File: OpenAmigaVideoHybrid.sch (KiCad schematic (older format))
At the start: 52 parts, among them J1 Conn_01x22, J99 OSHW_LOGO, Q1 2N3904, Q2 2N3904, Q3 2N3904, Q4 2N3904, Q5 2N3904, Q6 2N3906

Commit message: Begin migrating project to KiCad 5
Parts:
- removed C1, C2, C3, C4, C5: 100n, Capacitors_SMD:C_0805_HandSoldering, symbol C
- removed J1: Conn_01x22, OpenAmigaVideoHybrid:Pin_Header_Straight_1x22_Pitch2.54mm, symbol Conn_01x22
- removed J99: OSHW_LOGO, w_logo:Logo_copper_OSHW_6x6mm, symbol Conn_01x01
- removed Q1, Q2, Q3, Q4, Q5: 2N3904, OpenAmigaVideoHybrid:2N3904_2N3906_SOT-23, symbol 2N3904
- removed Q6: 2N3906, OpenAmigaVideoHybrid:2N3904_2N3906_SOT-23, symbol 2N3906
- removed R1, R17, R25, R9: 1k, Resistors_SMD:R_0805_HandSoldering, symbol R
- removed R10, R18, R2: 2k, Resistors_SMD:R_0805_HandSoldering, symbol R
- removed R11, R19, R3: 4k, Resistors_SMD:R_0805_HandSoldering, symbol R
- removed R12, R20, R4: 8k, Resistors_SMD:R_0805_HandSoldering, symbol R
- removed R13, R21, R5: 470, Resistors_SMD:R_0805_HandSoldering, symbol R
- removed R14, R22, R6: 390, Resistors_SMD:R_0805_HandSoldering, symbol R
- removed R15, R16, R23, R24, R29, R39, R7, R8: 75, Resistors_SMD:R_0805_HandSoldering, symbol R
- removed R26, R36: 220, Resistors_SMD:R_0805_HandSoldering, symbol R
- removed R27: 27k, Resistors_SMD:R_0805_HandSoldering, symbol R
- removed R28: 150, Resistors_SMD:R_0805_HandSoldering, symbol R
- removed R30: 90.9k, Resistors_SMD:R_0805_HandSoldering, symbol R
- removed R31, R34: 37.4k, Resistors_SMD:R_0805_HandSoldering, symbol R
- removed R32: 13.3k, Resistors_SMD:R_0805_HandSoldering, symbol R
- removed R33: 6.04k, Resistors_SMD:R_0805_HandSoldering, symbol R
- removed R35: 19.6k, Resistors_SMD:R_0805_HandSoldering, symbol R
- removed R37, R38: 36, Resistors_SMD:R_0805_HandSoldering, symbol R
- added C1, C2, C3, C4, C5: 100n, Capacitor_SMD:C_0805_2012Metric_Pad1.15x1.40mm_HandSolder, symbol Device:C
- added J1: CONN_MAINBOARD, Connector_PinHeader_2.54mm:PinHeader_1x22_P2.54mm_Vertical, symbol Connector:Conn_01x22_Male
- added Q1, Q2, Q3, Q4, Q5: 2N3904, OpenAmigaVideoHybrid:2N3904_2N3906_SOT-23, symbol Transistor_BJT:2N3904
- added Q6: 2N3906, OpenAmigaVideoHybrid:2N3904_2N3906_SOT-23, symbol Transistor_BJT:2N3906
- added R1, R17, R25, R9: 1k, Resistor_SMD:R_0805_2012Metric_Pad1.15x1.40mm_HandSolder, symbol Device:R
- added R10, R18, R2: 2k, Resistor_SMD:R_0805_2012Metric_Pad1.15x1.40mm_HandSolder, symbol Device:R
- added R11, R19, R3: 4k, Resistor_SMD:R_0805_2012Metric_Pad1.15x1.40mm_HandSolder, symbol Device:R
- added R12, R20, R4: 8k, Resistor_SMD:R_0805_2012Metric_Pad1.15x1.40mm_HandSolder, symbol Device:R
- added R13, R21, R5: 470, Resistor_SMD:R_0805_2012Metric_Pad1.15x1.40mm_HandSolder, symbol Device:R
- added R14, R22, R6: 390, Resistor_SMD:R_0805_2012Metric_Pad1.15x1.40mm_HandSolder, symbol Device:R
- added R15, R16, R23, R24, R29, R39, R7, R8: 75, Resistor_SMD:R_0805_2012Metric_Pad1.15x1.40mm_HandSolder, symbol Device:R
- added R26, R36: 220, Resistor_SMD:R_0805_2012Metric_Pad1.15x1.40mm_HandSolder, symbol Device:R
- added R27: 27k, Resistor_SMD:R_0805_2012Metric_Pad1.15x1.40mm_HandSolder, symbol Device:R
- added R28: 150, Resistor_SMD:R_0805_2012Metric_Pad1.15x1.40mm_HandSolder, symbol Device:R
- added R30: 90.9k, Resistor_SMD:R_0805_2012Metric_Pad1.15x1.40mm_HandSolder, symbol Device:R
- added R31, R34: 37.4k, Resistor_SMD:R_0805_2012Metric_Pad1.15x1.40mm_HandSolder, symbol Device:R
- added R32: 13.3k, Resistor_SMD:R_0805_2012Metric_Pad1.15x1.40mm_HandSolder, symbol Device:R
- added R33: 6.04k, Resistor_SMD:R_0805_2012Metric_Pad1.15x1.40mm_HandSolder, symbol Device:R
- added R35: 19.6k, Resistor_SMD:R_0805_2012Metric_Pad1.15x1.40mm_HandSolder, symbol Device:R
- added R37, R38: 36, Resistor_SMD:R_0805_2012Metric_Pad1.15x1.40mm_HandSolder, symbol Device:R
- added V0: OSHW_LOGO, Symbol:OSHW-Logo_5.7x6mm_Copper, symbol void:Void
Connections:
- wire segments 141 -> 197
- no-connect marks 1 -> 0

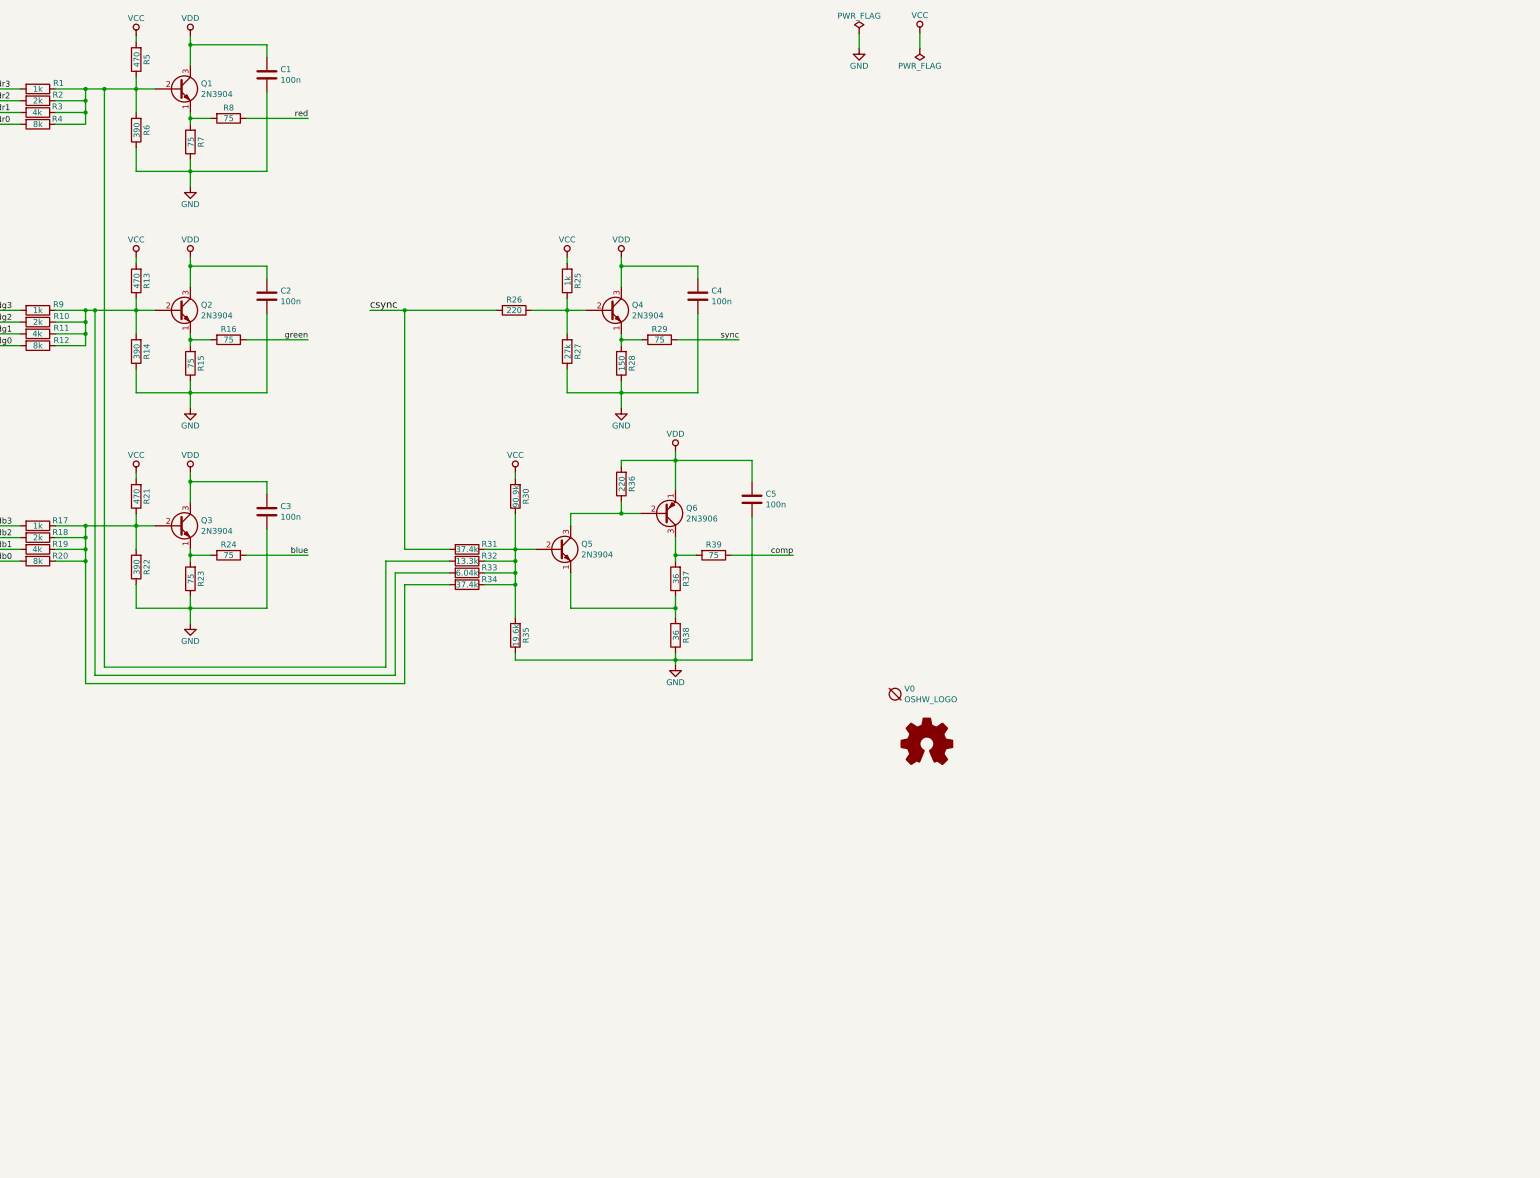
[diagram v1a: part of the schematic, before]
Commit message: Start working on color composite version
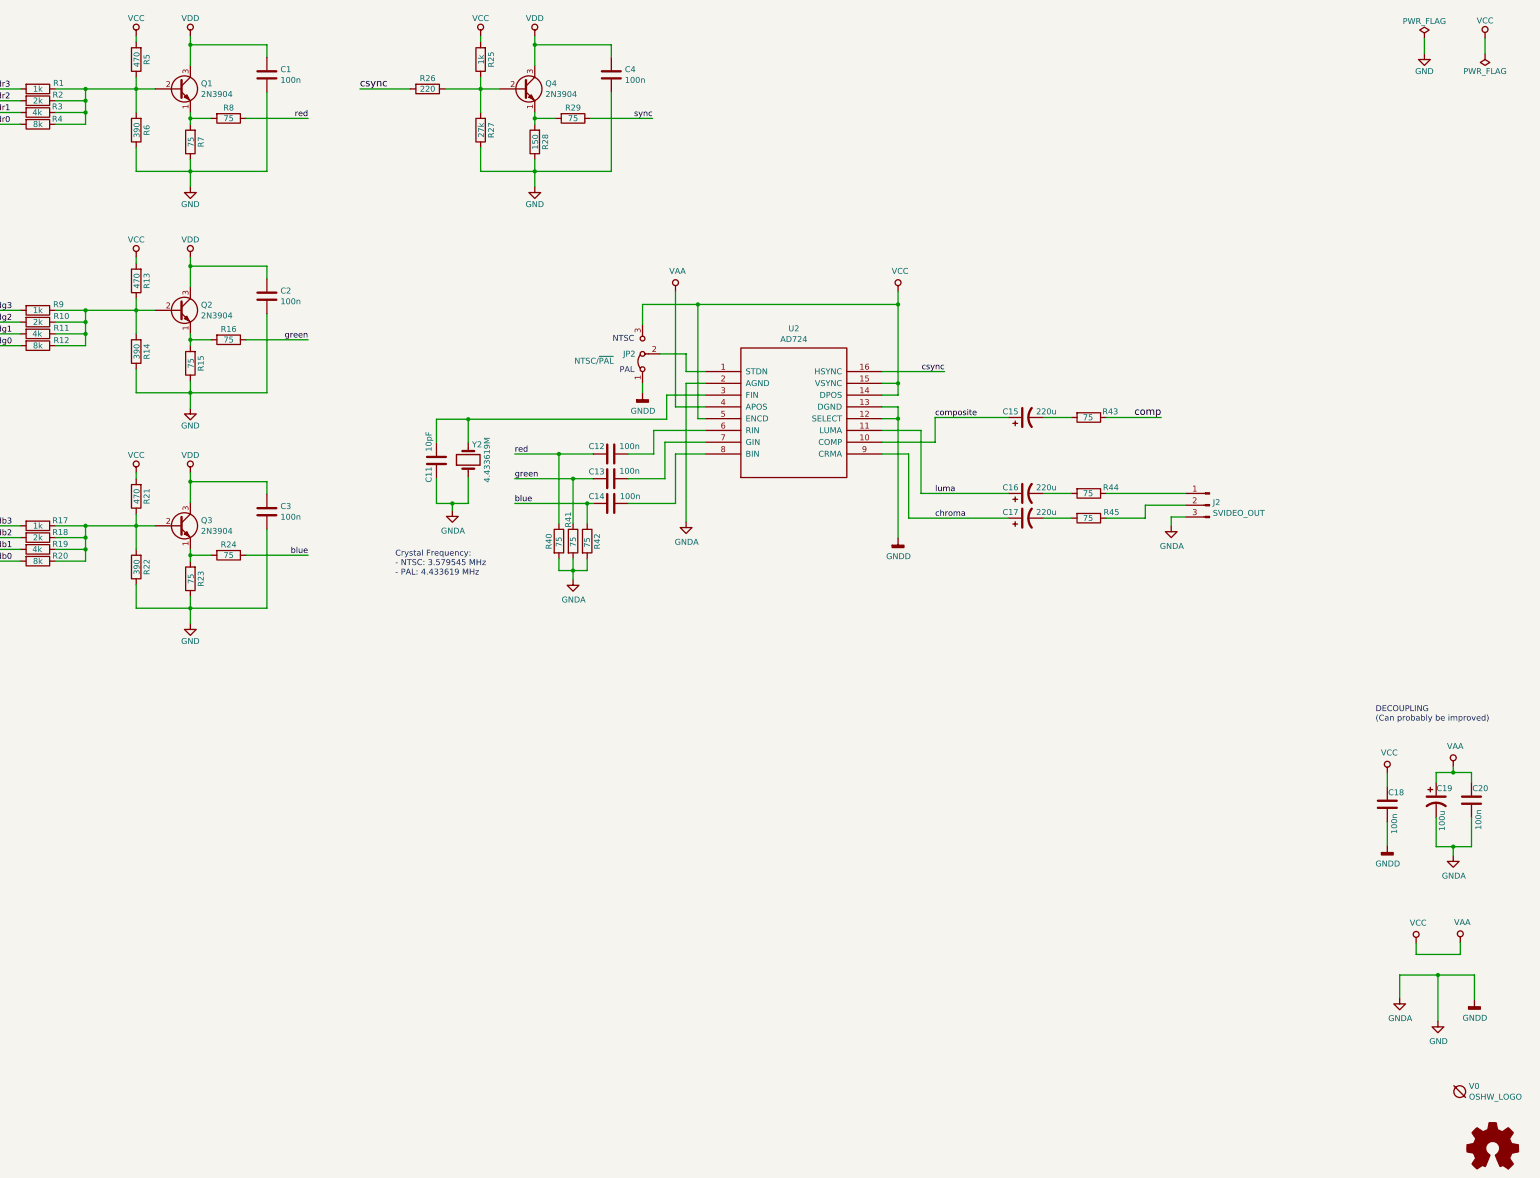
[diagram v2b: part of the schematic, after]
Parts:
- removed C5: 100n, Capacitor_SMD:C_0805_2012Metric_Pad1.15x1.40mm_HandSolder, symbol Device:C
- removed Q5: 2N3904, OpenAmigaVideoHybrid:2N3904_2N3906_SOT-23, symbol Transistor_BJT:2N3904
- removed Q6: 2N3906, OpenAmigaVideoHybrid:2N3904_2N3906_SOT-23, symbol Transistor_BJT:2N3906
- removed R30: 90.9k, Resistor_SMD:R_0805_2012Metric_Pad1.15x1.40mm_HandSolder, symbol Device:R
- removed R31, R34: 37.4k, Resistor_SMD:R_0805_2012Metric_Pad1.15x1.40mm_HandSolder, symbol Device:R
- removed R32: 13.3k, Resistor_SMD:R_0805_2012Metric_Pad1.15x1.40mm_HandSolder, symbol Device:R
- removed R33: 6.04k, Resistor_SMD:R_0805_2012Metric_Pad1.15x1.40mm_HandSolder, symbol Device:R
- removed R35: 19.6k, Resistor_SMD:R_0805_2012Metric_Pad1.15x1.40mm_HandSolder, symbol Device:R
- removed R36: 220, Resistor_SMD:R_0805_2012Metric_Pad1.15x1.40mm_HandSolder, symbol Device:R
- removed R37, R38: 36, Resistor_SMD:R_0805_2012Metric_Pad1.15x1.40mm_HandSolder, symbol Device:R
- removed R39: 75, Resistor_SMD:R_0805_2012Metric_Pad1.15x1.40mm_HandSolder, symbol Device:R
- added C11: 10pF, Capacitor_SMD:C_0805_2012Metric_Pad1.15x1.40mm_HandSolder, symbol Device:C
- added C12, C13, C14, C18: 100n, Capacitor_SMD:C_0805_2012Metric_Pad1.15x1.40mm_HandSolder, symbol Device:C
- added C15, C16, C17: 220u, Capacitor_SMD:CP_Elec_6.3x7.7, symbol Device:CP1
- added C19: 100u, Capacitor_SMD:CP_Elec_6.3x5.8, symbol Device:CP1
- added C20: 100n, Capacitor_SMD:C_1206_3216Metric_Pad1.42x1.75mm_HandSolder, symbol Device:C
- added J2: SVIDEO_OUT, Connector_PinHeader_2.54mm:PinHeader_1x03_P2.54mm_Vertical, symbol Connector:Conn_01x03_Male
- added JP2: NTSC/~PAL, OpenAmigaVideoHybrid:SolderJumper-3_P1.3mm_Bridged12_RoundedPad1.0x1.5mm, symbol Jumper:Jumper_3_Bridged12
- added R40, R41, R42, R43, R44, R45: 75, Resistor_SMD:R_0805_2012Metric_Pad1.15x1.40mm_HandSolder, symbol Device:R
- added U2: AD724, Package_SO:SOIC-16W_7.5x10.3mm_P1.27mm, symbol AD724:AD724
- added Y2: 4.433619M, Crystal:Crystal_HC49-4H_Vertical, symbol Device:Crystal
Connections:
- net labels added: GNDA, GNDD, VAA, chroma, composite, luma
- wire segments 197 -> 241
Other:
- note added: "Crystal Frequency:\n- NTSC: 3.579545 MHz\n- PAL: 4.433619 MHz"
- note added: "DECOUPLING\n(Can probably be improved)"
- note added: "NTSC"
- note added: "PAL"
- moved on the sheet: C4, Q4, R25, R26, R27, R28, R29, V0

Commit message: Almost there...
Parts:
- Y2: footprint Crystal:Crystal_HC49-4H_Vertical -> Crystal:Crystal_SMD_HC49-SD
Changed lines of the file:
@@
 F 0 "Y2" V 7150 4355 50  0000 C CNN
 F 1 "4.433619M" H 7020 4270 50  0000 C CNN
-F 2 "Crystal:Crystal_HC49-4H_Vertical" H 7020 4430 50  0001 C CNN
+F 2 "Crystal:Crystal_SMD_HC49-SD" H 7020 4430 50  0001 C CNN
 F 3 "~" H 7020 4430 50  0001 C CNN
 	1    7020 4430

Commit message: Even closer...
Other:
- moved on the sheet: J2
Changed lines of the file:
@@
 Wire Wire Line
 	12440 4715 13115 4715
-Wire Wire Line
-	13115 4915 12990 4915
-Wire Wire Line
-	12990 4915 12990 4990
 Text Label 12905 4070 2    60   ~ 0
 comp
@@
 L Connector:Conn_01x03_Male J?
 U 1 1 5EB9C6BC
-P 13315 4815
+P 13315 4715
 AR Path="/5EAF44C7/5EB9C6BC" Ref="J?"  Part="1"
 AR Path="/5EB9C6BC" Ref="J2"  Part="1"
-F 0 "J2" H 13287 4839 50  0000 R CNN
-F 1 "SVIDEO_OUT" H 13287 4748 50  0000 R CNN
-F 2 "Connector_PinHeader_2.54mm:PinHeader_1x03_P2.54mm_Vertical" H 13315 4815 50  0001 C CNN
-F 3 "~" H 13315 4815 50  0001 C CNN
-	1    13315 4815
-	-1   0    0    -1
+F 0 "J2" H 13287 4647 50  0000 R CNN
+F 1 "SVIDEO_OUT" H 13287 4738 50  0000 R CNN
+F 2 "Connector_PinHeader_2.54mm:PinHeader_1x03_P2.54mm_Vertical" H 13315 4715 50  0001 C CNN
+F 3 "~" H 13315 4715 50  0001 C CNN
+	1    13315 4715
+	-1   0    0    1
 $EndComp
 Wire Wire Line
@@
 	1    0    0    -1
 $EndComp
+Wire Wire Line
+	13115 4615 12990 4615
+Wire Wire Line
+	12990 4615 12990 4990
 $EndSCHEMATC

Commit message: Polish hybrid side
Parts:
- V0: footprint Symbol:OSHW-Logo_5.7x6mm_Copper -> OpenAmigaVideoHybrid:oshw_logo
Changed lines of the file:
@@
 F 0 "V0" H 15518 9841 50  0000 L CNN
 F 1 "OSHW_LOGO" H 15518 9750 50  0000 L CNN
-F 2 "Symbol:OSHW-Logo_5.7x6mm_Copper" H 15440 9795 50  0001 C CNN
+F 2 "OpenAmigaVideoHybrid:oshw_logo" H 15440 9795 50  0001 C CNN
 F 3 "" H 15440 9795 50  0001 C CNN
 	1    15440 9795

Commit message: Getting closer...
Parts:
- J2: footprint Connector_PinHeader_2.54mm:PinHeader_1x03_P2.54mm_Vertical -> OpenAmigaVideoHybrid:Pin_Header_Straight_1x03-ModSilkS
- renumbered JP2 to JP1, R40 to R30, R41 to R31, R42 to R32, R43 to R33, R44 to R34, R45 to R35, U2 to U1
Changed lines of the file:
@@
 P 9785 4030
 AR Path="/5EAF44C7/5EB9C56C" Ref="U?"  Part="1"
-AR Path="/5EB9C56C" Ref="U2"  Part="1"
-F 0 "U2" H 9785 4745 50  0000 C CNN
+AR Path="/5EB9C56C" Ref="U1"  Part="1"
+F 0 "U1" H 9785 4745 50  0000 C CNN
 F 1 "AD724" H 9785 4654 50  0000 C CNN
 F 2 "Package_SO:SOIC-16W_7.5x10.3mm_P1.27mm" H 9785 4030 50  0001 C CNN
@@
 P 7790 5120
 AR Path="/5EAF44C7/5EB9C595" Ref="R?"  Part="1"
-AR Path="/5EB9C595" Ref="R40"  Part="1"
-F 0 "R40" V 7705 5050 50  0000 L CNN
+AR Path="/5EB9C595" Ref="R30"  Part="1"
+F 0 "R30" V 7705 5050 50  0000 L CNN
 F 1 "75" V 7790 5070 50  0000 L CNN
 F 2 "Resistor_SMD:R_0805_2012Metric_Pad1.15x1.40mm_HandSolder" V 7720 5120 50  0001 C CNN
@@
 P 8030 5120
 AR Path="/5EAF44C7/5EB9C5A1" Ref="R?"  Part="1"
-AR Path="/5EB9C5A1" Ref="R42"  Part="1"
-F 0 "R42" V 8115 5050 50  0000 L CNN
+AR Path="/5EB9C5A1" Ref="R32"  Part="1"
+F 0 "R32" V 8115 5050 50  0000 L CNN
 F 1 "75" V 8030 5065 50  0000 L CNN
 F 2 "Resistor_SMD:R_0805_2012Metric_Pad1.15x1.40mm_HandSolder" V 7960 5120 50  0001 C CNN
@@
 P 8500 3530
 AR Path="/5EAF44C7/5EB9C5C5" Ref="JP?"  Part="1"
-AR Path="/5EB9C5C5" Ref="JP2"  Part="1"
-F 0 "JP2" V 8500 3590 50  0000 L CNN
+AR Path="/5EB9C5C5" Ref="JP1"  Part="1"
+F 0 "JP1" V 8500 3590 50  0000 L CNN
 F 1 "NTSC/~PAL" V 8440 3775 50  0000 L CNN
 F 2 "OpenAmigaVideoHybrid:SolderJumper-3_P1.3mm_Bridged12_RoundedPad1.0x1.5mm" H 8500 3530 50  0001 C CNN
@@
 P 12290 4070
 AR Path="/5EAF44C7/5EB9C67D" Ref="R?"  Part="1"
-AR Path="/5EB9C67D" Ref="R43"  Part="1"
-F 0 "R43" V 12240 4185 50  0000 L CNN
+AR Path="/5EB9C67D" Ref="R33"  Part="1"
+F 0 "R33" V 12240 4185 50  0000 L CNN
 F 1 "75" V 12290 4020 50  0000 L CNN
 F 2 "Resistor_SMD:R_0805_2012Metric_Pad1.15x1.40mm_HandSolder" V 12220 4070 50  0001 C CNN
@@
 P 12290 4925
 AR Path="/5EAF44C7/5EB9C689" Ref="R?"  Part="1"
-AR Path="/5EB9C689" Ref="R45"  Part="1"
-F 0 "R45" V 12240 5050 50  0000 L CNN
+AR Path="/5EB9C689" Ref="R35"  Part="1"
+F 0 "R35" V 12240 5050 50  0000 L CNN
 F 1 "75" V 12290 4875 50  0000 L CNN
 F 2 "Resistor_SMD:R_0805_2012Metric_Pad1.15x1.40mm_HandSolder" V 12220 4925 50  0001 C CNN
@@
 P 12290 4715
 AR Path="/5EAF44C7/5EB9C69B" Ref="R?"  Part="1"
-AR Path="/5EB9C69B" Ref="R44"  Part="1"
-F 0 "R44" V 12240 4835 50  0000 L CNN
+AR Path="/5EB9C69B" Ref="R34"  Part="1"
+F 0 "R34" V 12240 4835 50  0000 L CNN
 F 1 "75" V 12290 4665 50  0000 L CNN
 F 2 "Resistor_SMD:R_0805_2012Metric_Pad1.15x1.40mm_HandSolder" V 12220 4715 50  0001 C CNN
@@
 F 0 "J2" H 13287 4647 50  0000 R CNN
 F 1 "SVIDEO_OUT" H 13287 4738 50  0000 R CNN
-F 2 "Connector_PinHeader_2.54mm:PinHeader_1x03_P2.54mm_Vertical" H 13315 4715 50  0001 C CNN
+F 2 "OpenAmigaVideoHybrid:Pin_Header_Straight_1x03-ModSilkS" H 13315 4715 50  0001 C CNN
 F 3 "~" H 13315 4715 50  0001 C CNN
 	1    13315 4715
@@
 P 7910 5120
 AR Path="/5EAF44C7/5EB9C59B" Ref="R?"  Part="1"
-AR Path="/5EB9C59B" Ref="R41"  Part="1"
-F 0 "R41" V 7870 5235 50  0000 L CNN
+AR Path="/5EB9C59B" Ref="R31"  Part="1"
+F 0 "R31" V 7870 5235 50  0000 L CNN
 F 1 "75" V 7910 5070 50  0000 L CNN
 F 2 "Resistor_SMD:R_0805_2012Metric_Pad1.15x1.40mm_HandSolder" V 7840 5120 50  0001 C CNN

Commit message: Done!
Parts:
- renumbered C16 to C10, C17 to C11, C18 to C12, C19 to C13, C20 to C14, C11 to C5, C12 to C6, C13 to C7, C14 to C8, C15 to C9, Y2 to Y1
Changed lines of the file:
@@
 Sheet 1 1
 Title "OpenAmigaVideoHybrid"
-Date "2020-03-31"
+Date "2020-04-01"
 Rev "2git"
 Comp "SukkoPera"
@@
 P 8230 4380
 AR Path="/5EAF44C7/5EB9C574" Ref="C?"  Part="1"
-AR Path="/5EB9C574" Ref="C12"  Part="1"
-F 0 "C12" V 8165 4260 50  0000 C CNN
+AR Path="/5EB9C574" Ref="C6"  Part="1"
+F 0 "C6" V 8165 4260 50  0000 C CNN
 F 1 "100n" V 8165 4540 50  0000 C CNN
 F 2 "Capacitor_SMD:C_0805_2012Metric_Pad1.15x1.40mm_HandSolder" H 8268 4230 50  0001 C CNN
@@
 P 8230 4590
 AR Path="/5EAF44C7/5EB9C57A" Ref="C?"  Part="1"
-AR Path="/5EB9C57A" Ref="C13"  Part="1"
-F 0 "C13" V 8170 4470 50  0000 C CNN
+AR Path="/5EB9C57A" Ref="C7"  Part="1"
+F 0 "C7" V 8170 4470 50  0000 C CNN
 F 1 "100n" V 8165 4750 50  0000 C CNN
 F 2 "Capacitor_SMD:C_0805_2012Metric_Pad1.15x1.40mm_HandSolder" H 8268 4440 50  0001 C CNN
@@
 P 8230 4800
 AR Path="/5EAF44C7/5EB9C580" Ref="C?"  Part="1"
-AR Path="/5EB9C580" Ref="C14"  Part="1"
-F 0 "C14" V 8170 4680 50  0000 C CNN
+AR Path="/5EB9C580" Ref="C8"  Part="1"
+F 0 "C8" V 8170 4680 50  0000 C CNN
 F 1 "100n" V 8170 4965 50  0000 C CNN
 F 2 "Capacitor_SMD:C_0805_2012Metric_Pad1.15x1.40mm_HandSolder" H 8268 4650 50  0001 C CNN
@@
 P 7020 4430
 AR Path="/5EAF44C7/5EB9C5CD" Ref="Y?"  Part="1"
-AR Path="/5EB9C5CD" Ref="Y2"  Part="1"
-F 0 "Y2" V 7150 4355 50  0000 C CNN
+AR Path="/5EB9C5CD" Ref="Y1"  Part="1"
+F 0 "Y1" V 7150 4355 50  0000 C CNN
 F 1 "4.433619M" H 7020 4270 50  0000 C CNN
 F 2 "Crystal:Crystal_SMD_HC49-SD" H 7020 4430 50  0001 C CNN
@@
 P 6750 4435
 AR Path="/5EAF44C7/5EB9C5D4" Ref="C?"  Part="1"
-AR Path="/5EB9C5D4" Ref="C11"  Part="1"
-F 0 "C11" V 6685 4315 50  0000 C CNN
+AR Path="/5EB9C5D4" Ref="C5"  Part="1"
+F 0 "C5" V 6685 4315 50  0000 C CNN
 F 1 "10pF" V 6685 4595 50  0000 C CNN
 F 2 "Capacitor_SMD:C_0805_2012Metric_Pad1.15x1.40mm_HandSolder" H 6788 4285 50  0001 C CNN
@@
 P 15240 7320
 AR Path="/5EAF44C7/5EB9C623" Ref="C?"  Part="1"
-AR Path="/5EB9C623" Ref="C19"  Part="1"
-F 0 "C19" H 15310 7420 50  0000 C CNN
+AR Path="/5EB9C623" Ref="C13"  Part="1"
+F 0 "C13" H 15310 7420 50  0000 C CNN
 F 1 "100u" V 15290 7145 50  0000 C CNN
 F 2 "Capacitor_SMD:CP_Elec_6.3x5.8" H 15240 7320 50  0001 C CNN
@@
 P 15540 7320
 AR Path="/5EAF44C7/5EB9C629" Ref="C?"  Part="1"
-AR Path="/5EB9C629" Ref="C20"  Part="1"
-F 0 "C20" H 15465 7220 50  0000 C CNN
+AR Path="/5EB9C629" Ref="C14"  Part="1"
+F 0 "C14" H 15465 7220 50  0000 C CNN
 F 1 "100n" V 15480 7485 50  0000 C CNN
 F 2 "Capacitor_SMD:C_1206_3216Metric_Pad1.42x1.75mm_HandSolder" H 15578 7170 50  0001 C CNN
@@
 P 14825 7355
 AR Path="/5EAF44C7/5EB9C63B" Ref="C?"  Part="1"
-AR Path="/5EB9C63B" Ref="C18"  Part="1"
-F 0 "C18" H 14750 7255 50  0000 C CNN
+AR Path="/5EB9C63B" Ref="C12"  Part="1"
+F 0 "C12" H 14750 7255 50  0000 C CNN
 F 1 "100n" V 14765 7520 50  0000 C CNN
 F 2 "Capacitor_SMD:C_0805_2012Metric_Pad1.15x1.40mm_HandSolder" H 14863 7205 50  0001 C CNN
@@
 P 11755 4070
 AR Path="/5EAF44C7/5EB9C683" Ref="C?"  Part="1"
-AR Path="/5EB9C683" Ref="C15"  Part="1"
-F 0 "C15" V 11805 4200 50  0000 C CNN
+AR Path="/5EB9C683" Ref="C9"  Part="1"
+F 0 "C9" V 11805 4200 50  0000 C CNN
 F 1 "220u" V 11805 3895 50  0000 C CNN
 F 2 "Capacitor_SMD:CP_Elec_6.3x7.7" H 11755 4070 50  0001 C CNN
@@
 P 11755 4925
 AR Path="/5EAF44C7/5EB9C695" Ref="C?"  Part="1"
-AR Path="/5EB9C695" Ref="C17"  Part="1"
-F 0 "C17" V 11805 5055 50  0000 C CNN
+AR Path="/5EB9C695" Ref="C11"  Part="1"
+F 0 "C11" V 11805 5055 50  0000 C CNN
 F 1 "220u" V 11805 4750 50  0000 C CNN
 F 2 "Capacitor_SMD:CP_Elec_6.3x7.7" H 11755 4925 50  0001 C CNN
@@
 P 11755 4715
 AR Path="/5EAF44C7/5EB9C6A1" Ref="C?"  Part="1"
-AR Path="/5EB9C6A1" Ref="C16"  Part="1"
-F 0 "C16" V 11805 4845 50  0000 C CNN
+AR Path="/5EB9C6A1" Ref="C10"  Part="1"
+F 0 "C10" V 11805 4845 50  0000 C CNN
 F 1 "220u" V 11805 4540 50  0000 C CNN
 F 2 "Capacitor_SMD:CP_Elec_6.3x7.7" H 11755 4715 50  0001 C CNN
